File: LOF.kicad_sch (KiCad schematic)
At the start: 1 part

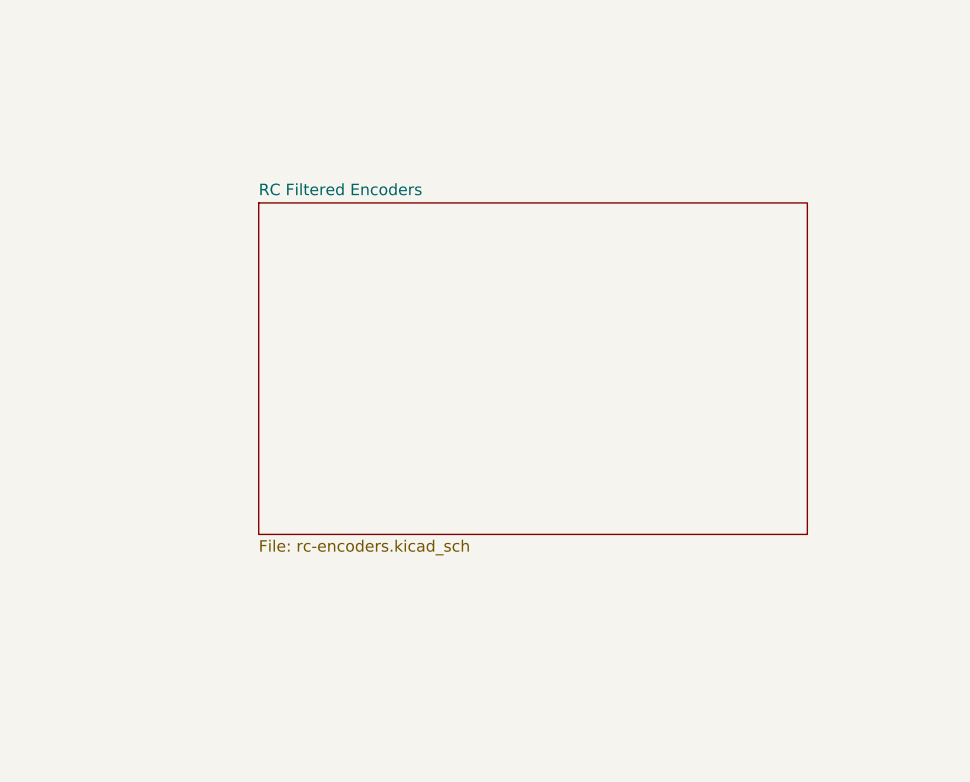
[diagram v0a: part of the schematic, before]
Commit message: Added rest of the encoder terminal to hierarchical sheets
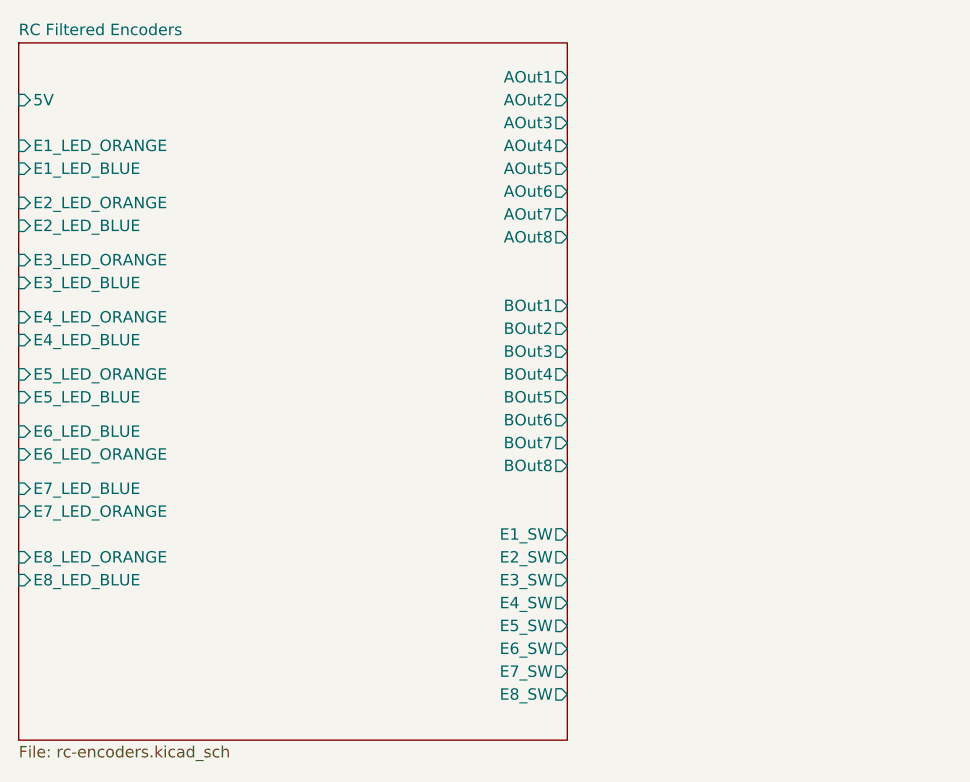
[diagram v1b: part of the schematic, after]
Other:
- sheet RC Filtered Encoders ports: added 5V, AOut1, AOut2, AOut3, AOut4, AOut5, AOut6, AOut7, AOut8, BOut1, BOut2, BOut3, BOut4, BOut5, BOut6, BOut7, BOut8, E1_LED_BLUE, E1_LED_ORANGE, E1_SW, E2_LED_BLUE, E2_LED_ORANGE, E2_SW, E3_LED_BLUE, E3_LED_ORANGE, E3_SW, E4_LED_BLUE, E4_LED_ORANGE, E4_SW, E5_LED_BLUE, E5_LED_ORANGE, E5_SW, E6_LED_BLUE, E6_LED_ORANGE, E6_SW, E7_LED_BLUE, E7_LED_ORANGE, E7_SW, E8_LED_BLUE, E8_LED_ORANGE, E8_SW; removed none

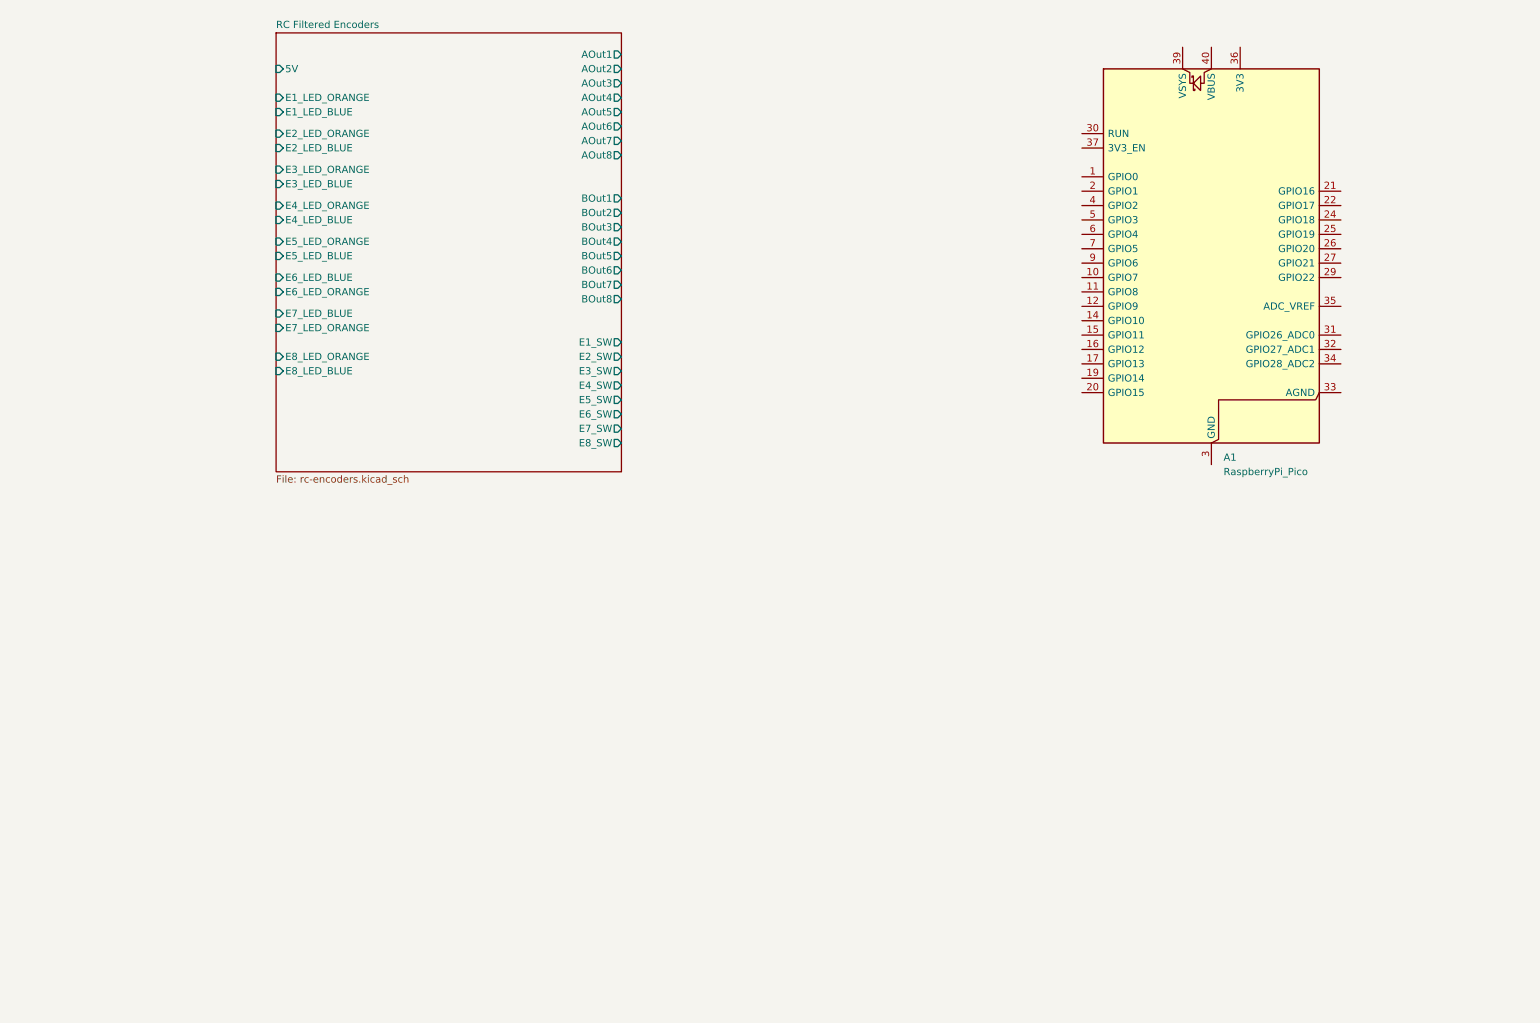
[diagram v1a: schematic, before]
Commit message: Added variable resistor and switches
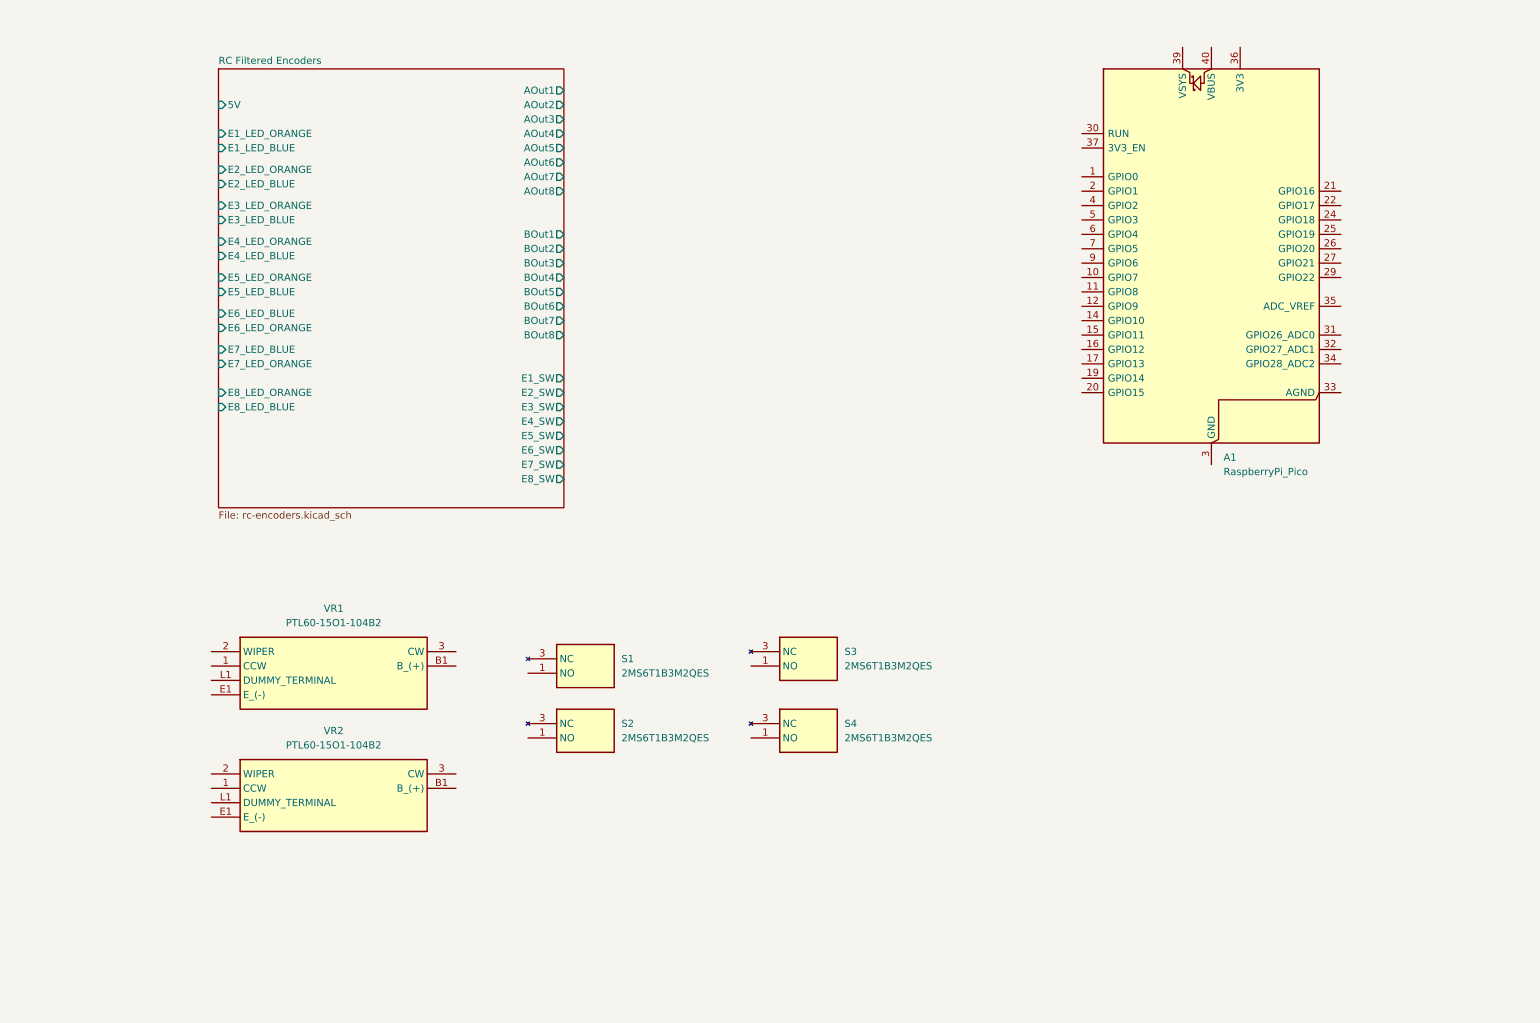
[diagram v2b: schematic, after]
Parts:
- added S1, S2, S3, S4: 2MS6T1B3M2QES, 2MS6T1B3M2QES, symbol SamacSys_Parts:2MS6T1B3M2QES
- added VR1, VR2: PTL60-15O1-104B2, PTL6015O1104B2, symbol SamacSys_Parts:PTL60-15O1-104B2

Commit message: Update schematic
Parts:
- added J1: EXT_3.3V, Connector_Wire:SolderWire-0.75sqmm_1x01_D1.25mm_OD3.5mm_Relief, symbol Connector_Generic:Conn_01x01
- added J2: VBUS_IN, Connector_Wire:SolderWire-0.75sqmm_1x01_D1.25mm_OD3.5mm_Relief, symbol Connector_Generic:Conn_01x01
- added J3: GND, Connector_Wire:SolderWire-0.75sqmm_1x01_D1.25mm_OD3.5mm_Relief, symbol Connector_Generic:Conn_01x01
- added U1: 815, Kicad Libs:MODULE_815, symbol 815:815
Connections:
- net GND: now reaches S1.1 (NO)
- net GND: now also S2.1 (NO), S3.1 (NO), S4.1 (NO), VR1.1 (CCW), VR1.E1 (E_(-)), VR2.1 (CCW), VR2.E1 (E_(-)), J3.1 (Pin_1), U1.GND_1 (GND)
- net S1_NC: now reaches S1.3 (NC)
- net S1_NC: now also A1.24 (GPIO18)
- net S3_NC: now reaches S3.3 (NC)
- net S3_NC: now also A1.26 (GPIO20)
- net AOut1: now reaches A1.1 (GPIO0)
- net BOut3: now reaches A1.10 (GPIO7)
- net AOut4: now reaches A1.11 (GPIO8)
- net BOut4: now reaches A1.12 (GPIO9)
- net AOut5: now reaches A1.14 (GPIO10)
- net BOut5: now reaches A1.15 (GPIO11)
- net AOut6: now reaches A1.16 (GPIO12)
- net BOut6: now reaches A1.17 (GPIO13)
- net AOut7: now reaches A1.19 (GPIO14)
- net BOut1: now reaches A1.2 (GPIO1)
- net BOut7: now reaches A1.20 (GPIO15)
- net AOut8: now reaches A1.21 (GPIO16)
- net BOut8: now reaches A1.22 (GPIO17)
- net S2_NC: now reaches A1.25 (GPIO19)
- net S2_NC: now also S2.3 (NC)
- net S4_NC: now reaches A1.27 (GPIO21)
- net S4_NC: now also S4.3 (NC)
- net WIPER_VR1: now reaches A1.31 (GPIO26_ADC0)
- net WIPER_VR1: now also VR1.2 (WIPER)
- net WIPER_VR2: now reaches A1.32 (GPIO27_ADC1)
- net WIPER_VR2: now also VR2.2 (WIPER)
- net 3V3: now reaches A1.36 (3V3)
- net 3V3: now also U1.VCC_1 (VCC)
- net AOut2: now reaches A1.4 (GPIO2)
- net VBUS: now reaches A1.40 (VBUS)
- net BOut2: now reaches A1.5 (GPIO3)
- net SDA: now reaches A1.6 (GPIO4)
- net SDA: now also U1.SDA_1 (SDA)
- net SCL: now reaches A1.7 (GPIO5)
- net SCL: now also U1.SCL_1 (SCL)
- net AOut3: now reaches A1.9 (GPIO6)
- net +3.3V: now reaches VR1.3 (CW)
- net +3.3V: now also VR2.3 (CW)
- net EXT_3.3V: now reaches VR1.B1 (B_(+))
- net EXT_3.3V: now also VR2.B1 (B_(+)), J1.1 (Pin_1), U1.V+_1 (V+)
- new net E1_LED_BLUE: U1.1 (PWM_1)
- new net E1_LED_ORANGE: U1.0 (PWM_0)
- new net E2_LED_BLUE: U1.3 (PWM_3)
- new net E2_LED_ORANGE: U1.2 (PWM_2)
- new net E3_LED_BLUE: U1.5 (PWM_5)
- new net E3_LED_ORANGE: U1.4 (PWM_4)
- new net E4_LED_BLUE: U1.7 (PWM_7)
- new net E4_LED_ORANGE: U1.6 (PWM_6)
- new net E5_LED_BLUE: U1.9 (PWM_9)
- new net E5_LED_ORANGE: U1.8 (PWM_8)
- new net E6_LED_BLUE: U1.10 (PWM_10)
- new net E6_LED_ORANGE: U1.11 (PWM_11)
- new net E7_LED_BLUE: U1.12 (PWM_12)
- new net E7_LED_ORANGE: U1.13 (PWM_13)
- new net E8_LED_BLUE: U1.15 (PWM_15)
- new net E8_LED_ORANGE: U1.14 (PWM_14)
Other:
- sheet RC Filtered Encoders ports: added 3.3V; removed 5V
- moved on the sheet: A1, S1, S2, S3, S4, VR1, VR2

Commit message: Made fixes according to the erc
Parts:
- removed U1: 815, Kicad Libs:MODULE_815, symbol 815:815
- added J10, J11, J12, J13, J14, J15, J16, J17, J18, J19, J20, J21, J22, J23, J24, J25, J4, J5, J6, J7, J8, J9: Conn_01x01, Connector_Wire:SolderWire-0.25sqmm_1x01_D0.65mm_OD1.7mm, symbol Connector_Generic:Conn_01x01
- J1: value EXT_3.3V -> Conn_01x01; footprint Connector_Wire:SolderWire-0.75sqmm_1x01_D1.25mm_OD3.5mm_Relief -> Connector_Wire:SolderWire-0.25sqmm_1x01_D0.65mm_OD1.7mm
- J2: value VBUS_IN -> Conn_01x01; footprint Connector_Wire:SolderWire-0.75sqmm_1x01_D1.25mm_OD3.5mm_Relief -> Connector_Wire:SolderWire-0.25sqmm_1x01_D0.65mm_OD1.7mm
- J3: value GND -> Conn_01x01; footprint Connector_Wire:SolderWire-0.75sqmm_1x01_D1.25mm_OD3.5mm_Relief -> Connector_Wire:SolderWire-0.25sqmm_1x01_D0.65mm_OD1.7mm
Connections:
- net +3.3V is gone; now on net 3V3: VR1.3 (CW), VR2.3 (CW)
- net 3V3: now also J1.1 (Pin_1)
- net GND: now also A1.33 (AGND), VR1.L1 (DUMMY_TERMINAL), VR2.L1 (DUMMY_TERMINAL), J22.1 (Pin_1), J25.1 (Pin_1); no longer J3.1 (Pin_1)
- net SCL: now also J19.1 (Pin_1)
- net SDA: now also J20.1 (Pin_1)
- net VBUS: now also J24.1 (Pin_1)
- net OE: now reaches A1.29 (GPIO22)
- net OE: now also J21.1 (Pin_1)
- net LED_VCC: now reaches J2.1 (Pin_1)
- net LED_VCC: now also VR1.B1 (B_(+)), VR2.B1 (B_(+)), J23.1 (Pin_1)
- removed net EXT_3.3V: J1.1 (Pin_1), VR1.B1 (B_(+)), VR2.B1 (B_(+))
- net S1_NC renamed GPIO18
- net S2_NC renamed GPIO19
- net S3_NC renamed GPIO20
- net S4_NC renamed GPIO21
- new net PWM_0: J3.1 (Pin_1)
- new net PWM_1: J4.1 (Pin_1)
- new net PWM_10: J13.1 (Pin_1)
- new net PWM_11: J14.1 (Pin_1)
- new net PWM_12: J15.1 (Pin_1)
- new net PWM_13: J16.1 (Pin_1)
- new net PWM_14: J17.1 (Pin_1)
- new net PWM_15: J18.1 (Pin_1)
- new net PWM_2: J5.1 (Pin_1)
- new net PWM_3: J6.1 (Pin_1)
- new net PWM_4: J7.1 (Pin_1)
- new net PWM_5: J8.1 (Pin_1)
- new net PWM_6: J9.1 (Pin_1)
- new net PWM_7: J10.1 (Pin_1)
- new net PWM_8: J11.1 (Pin_1)
- new net PWM_9: J12.1 (Pin_1)
- no-connect marks 0 -> 6
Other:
- sheet RC Filtered Encoders ports: added none; removed E1_SW, E2_SW, E3_SW, E4_SW, E5_SW, E6_SW, E7_SW, E8_SW
- moved on the sheet: VR1, VR2

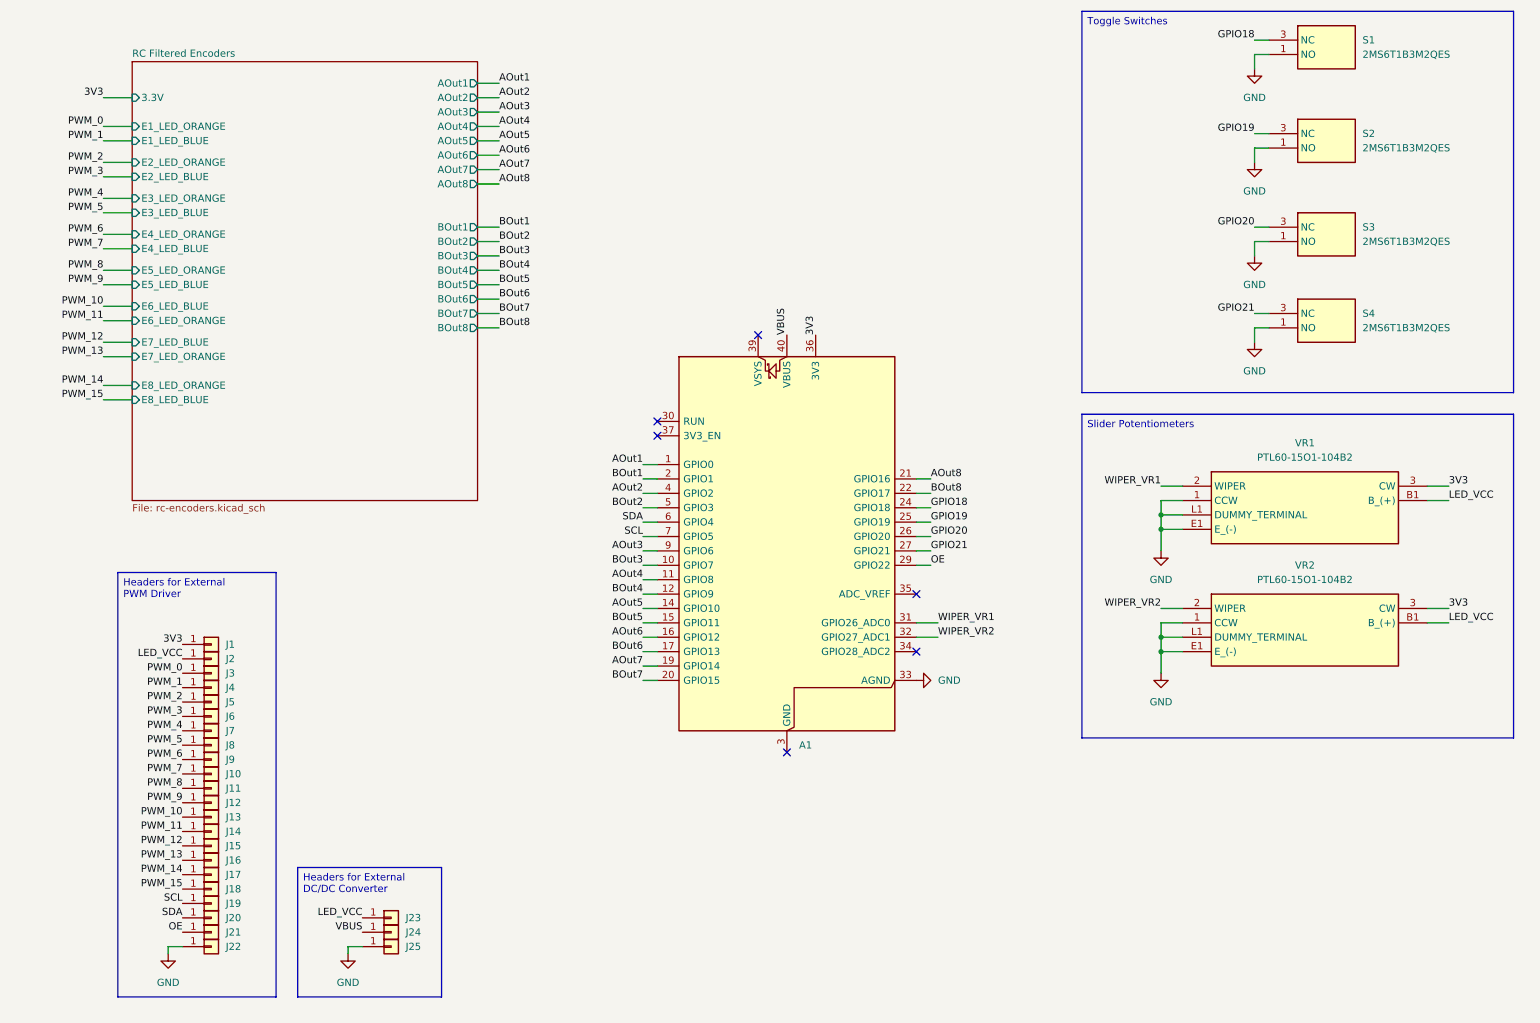
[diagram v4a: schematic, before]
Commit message: All components and footprints set
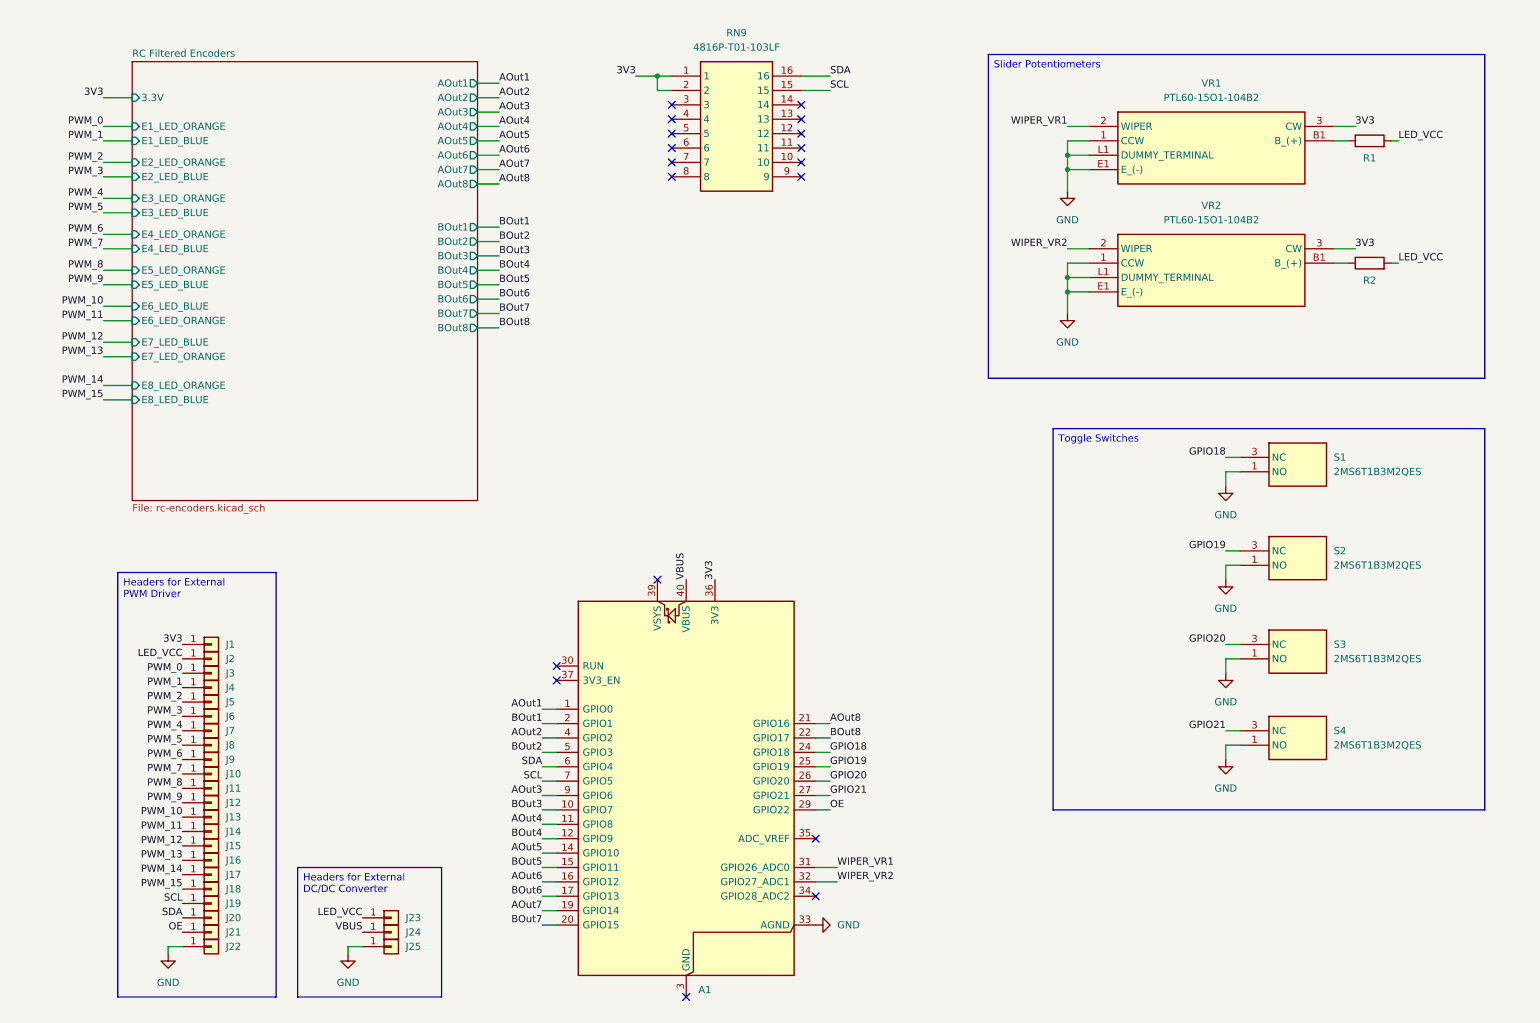
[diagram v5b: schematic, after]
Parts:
- added R1, R2: R, Resistor_THT:R_Axial_DIN0207_L6.3mm_D2.5mm_P10.16mm_Horizontal, symbol Device:R
- added RN9: 4816P-T01-103LF, SamacSys_Parts:SOIC127P762X215-16N, symbol SamacSys_Parts:4816P-T01-103LF
- S1, S2, S3, S4: footprint 2MS6T1B3M2QES -> SamacSys_Parts:2MS6T1B3M2QES
- VR1, VR2: footprint PTL6015O1104B2 -> SamacSys_Parts:PTL6015O1104B2
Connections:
- net 3V3: now also RN9.1, RN9.2
- net LED_VCC: now also R1.2, R2.2; no longer VR1.B1 (B_(+)), VR2.B1 (B_(+))
- net SCL: now also RN9.15
- net SDA: now also RN9.16
- new net: R1.1, VR1.B1 (B_(+))
- new net: R2.1, VR2.B1 (B_(+))
- no-connect marks 6 -> 18
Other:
- moved on the sheet: A1, S1, S2, S3, S4, VR1, VR2
